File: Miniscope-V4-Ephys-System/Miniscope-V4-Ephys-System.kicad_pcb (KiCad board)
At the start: 4 copper layers, 58.8 x 47 mm, 150 parts, among them J1 34 Circuit Slimslack Connector, J10 Conn_01x01, J11 Conn_01x01, J12 Conn_01x01, J13 Conn_01x01, J14 Conn_01x05, J15 Conn_01x01, J16 Conn_01x01, J17 Conn_01x01, J18 Conn_01x01, J19 Conn_01x01, J2 Conn_01x01, J20 Conn_01x01, J21 Conn_01x01, J22 Conn_01x01, J23 Conn_01x01, J24 Conn_01x01, J25 Conn_01x01, J26 Conn_01x01, J27 Conn_01x01, J28 Conn_01x01, J3 Conn_01x01, J4 Conn_01x01, J5 Conn_01x01, J6 Conn_01x01, J7 Conn_01x01, J8 Conn_01x01, J9 Conn_01x01, Q1 MMBT3904LP-7B, U1 RHD2132, U2 TXB0304RUT, U3 MCP1711T-30I/5X, U4 ATSAME70N21A-CN, U5 MCP1711T-18I/5X, Y1 SMD_CRYSTAL

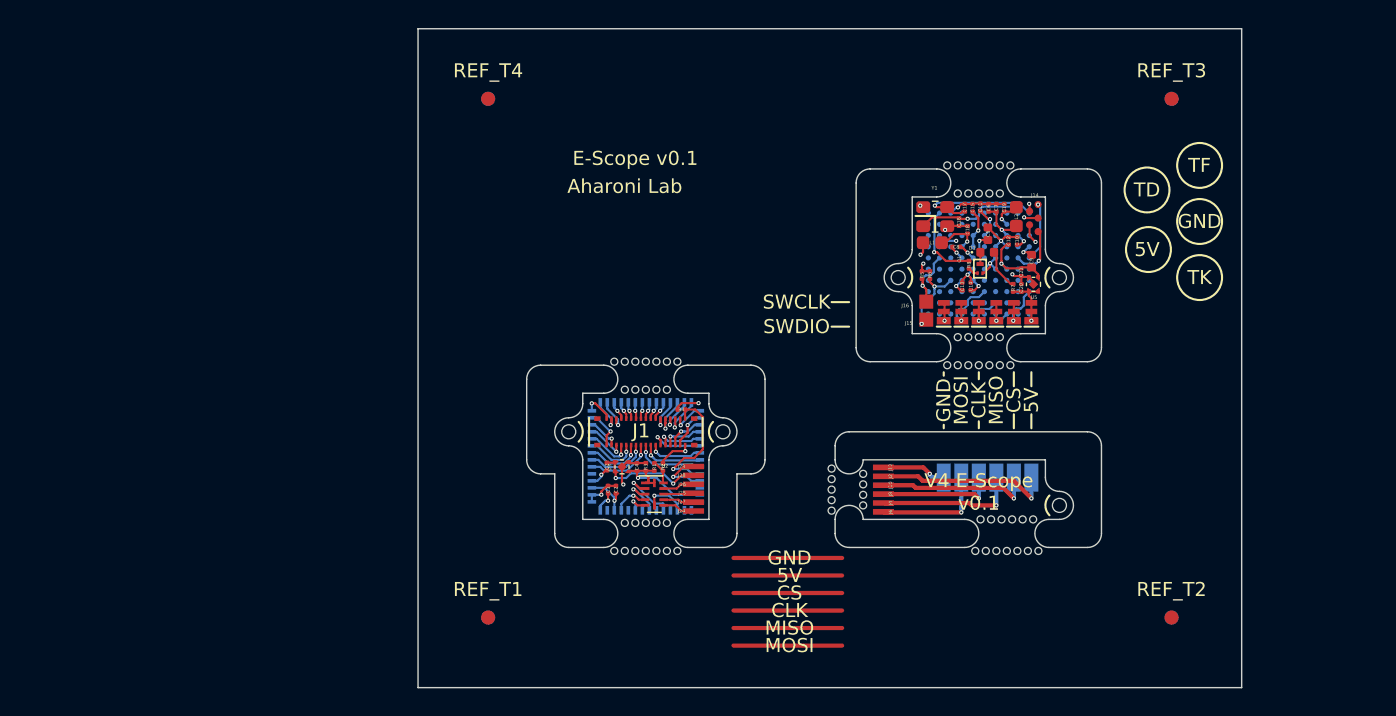
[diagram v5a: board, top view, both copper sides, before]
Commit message: Add programing board and generate GERBERS for fab (v0.1)
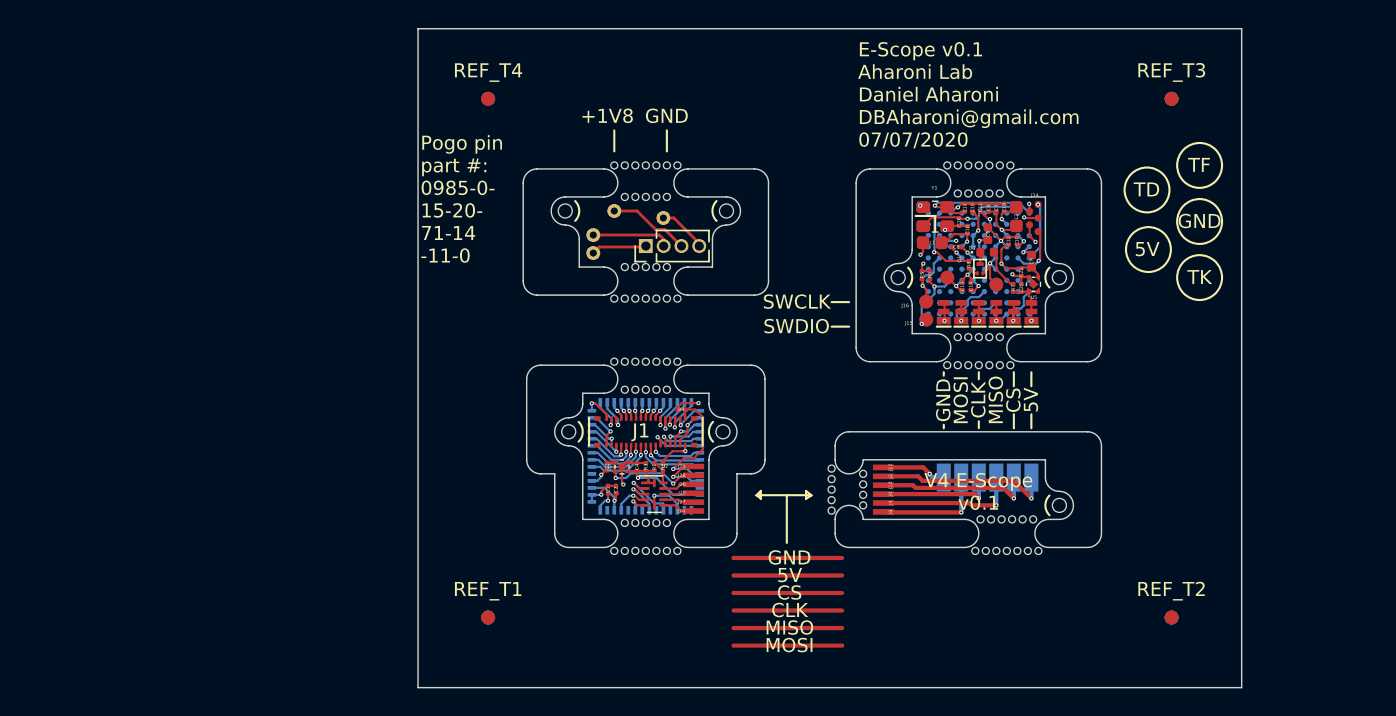
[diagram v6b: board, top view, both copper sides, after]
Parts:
- added HOLE: Conn_1x1_700_Circular_Pad, .Connector:Conn_1x1_700_Circular_Pad, F.Cu at (112.8, 119.2)
- added HOLE: Conn_1x1_700_Circular_Pad, .Connector:Conn_1x1_700_Circular_Pad, F.Cu at (110.5, 117.0)
- added HOLE: Conn_1x1_700_Circular_Pad, .Connector:Conn_1x1_700_Circular_Pad, F.Cu at (112.0, 117.0)
- added HOLE: Conn_1x1_700_Circular_Pad, .Connector:Conn_1x1_700_Circular_Pad, F.Cu at (112.8, 117.0)
- added HOLE: Conn_1x1_700_Circular_Pad, .Connector:Conn_1x1_700_Circular_Pad, F.Cu at (111.2, 117.0)
- added HOLE: Conn_1x1_700_Circular_Pad, .Connector:Conn_1x1_700_Circular_Pad, F.Cu at (109.8, 109.8)
- added HOLE: Conn_1x1_700_Circular_Pad, .Connector:Conn_1x1_700_Circular_Pad, F.Cu at (112.8, 112.0)
- added HOLE: Conn_1x1_700_Circular_Pad, .Connector:Conn_1x1_700_Circular_Pad, F.Cu at (110.5, 112.0)
- added HOLE: Conn_1x1_700_Circular_Pad, .Connector:Conn_1x1_700_Circular_Pad, F.Cu at (112.8, 109.8)
- added HOLE: Conn_1x1_700_Circular_Pad, .Connector:Conn_1x1_700_Circular_Pad, F.Cu at (111.2, 109.8)
- added HOLE: Conn_1x1_700_Circular_Pad, .Connector:Conn_1x1_700_Circular_Pad, F.Cu at (112.0, 109.8)
- added HOLE: Conn_1x1_700_Circular_Pad, .Connector:Conn_1x1_700_Circular_Pad, F.Cu at (112.0, 119.2)
- added HOLE: Conn_1x1_700_Circular_Pad, .Connector:Conn_1x1_700_Circular_Pad, F.Cu at (112.0, 112.0)
- added HOLE: Conn_1x1_700_Circular_Pad, .Connector:Conn_1x1_700_Circular_Pad, F.Cu at (110.5, 109.8)
- added HOLE: Conn_1x1_700_Circular_Pad, .Connector:Conn_1x1_700_Circular_Pad, F.Cu at (109.8, 112.0)
- added HOLE: Conn_1x1_700_Circular_Pad, .Connector:Conn_1x1_700_Circular_Pad, F.Cu at (111.2, 112.0)
- added HOLE: Conn_1x1_700_Circular_Pad, .Connector:Conn_1x1_700_Circular_Pad, F.Cu at (109.0, 109.8)
- added HOLE: Conn_1x1_700_Circular_Pad, .Connector:Conn_1x1_700_Circular_Pad, F.Cu at (105.5, 113.0)
- added HOLE: Conn_1x1_700_Circular_Pad, .Connector:Conn_1x1_700_Circular_Pad, F.Cu at (117.0, 113.0)
- added HOLE: Conn_1x1_700_Circular_Pad, .Connector:Conn_1x1_700_Circular_Pad, F.Cu at (109.0, 119.2)
- added HOLE: Conn_1x1_700_Circular_Pad, .Connector:Conn_1x1_700_Circular_Pad, F.Cu at (113.5, 119.2)
- added HOLE: Conn_1x1_700_Circular_Pad, .Connector:Conn_1x1_700_Circular_Pad, F.Cu at (111.2, 119.2)
- added HOLE: Conn_1x1_700_Circular_Pad, .Connector:Conn_1x1_700_Circular_Pad, F.Cu at (110.5, 119.2)
- added HOLE: Conn_1x1_700_Circular_Pad, .Connector:Conn_1x1_700_Circular_Pad, F.Cu at (109.8, 119.2)
- added HOLE: Conn_1x1_700_Circular_Pad, .Connector:Conn_1x1_700_Circular_Pad, F.Cu at (109.8, 117.0)
- added HOLE: Conn_1x1_700_Circular_Pad, .Connector:Conn_1x1_700_Circular_Pad, F.Cu at (113.5, 109.8)
- added J15: Conn_01x01, .Connector:Conn_1x1_250x750_Pad, F.Cu at (107.5, 116.0)
- added J16: Conn_01x01, .Connector:Conn_1x1_250x750_Pad, F.Cu at (107.5, 114.7)
- added J_programming: PinHeader_1x04_P1.27mm_Vertical, Connector_PinHeader_1.27mm:PinHeader_1x04_P1.27mm_Vertical, F.Cu at (111.2, 115.5)
- added TP_1V8: Conn_1x1_250x750_Pad, .Connector:Conn_1x1_100x100_Pad, F.Cu at (112.5, 113.5)
- added TP_1V8: Conn_1x1_250x750_Pad, .Connector:Conn_1x1_100x100_Pad, F.Cu at (109.0, 113.0)
- added TP_1V8: Conn_1x1_250x750_Pad, .Connector:Conn_1x1_100x100_Pad, F.Cu at (132.8, 117.8)
- added TP_GND: Conn_1x1_250x750_Pad, .Connector:Conn_1x1_100x100_Pad, F.Cu at (136.2, 118.2)
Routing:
- net (no net): track 0.00 -> 18.9 mm
- net GND: track 45.9 -> 47.6 mm
- net +1V8: track 14.4 -> 15.3 mm
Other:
- outline, holes or cut-outs redrawn
- board text added: "+1V8"
- board text added: "E-Scope v0.1 Aharoni Lab Daniel Aharoni DBAharoni@gmail.com 07/07/2020"
- board text added: "Pogo pin part #: 0985-0- 15-20- 71-14 -11-0"
- board text removed: "Aharoni Lab"
- board text removed: "E-Scope v0.1"
